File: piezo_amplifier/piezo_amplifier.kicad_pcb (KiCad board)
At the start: 2 copper layers, 40 x 23.5 mm, 22 parts, among them J1 Conn_01x02_Female, J2 Conn_01x02_Female, J3 Conn_01x02_Female, J4 Conn_01x02_Female, U1 LMV324, U2 TLV76033DBZT

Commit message: Add Logo on silkscreen
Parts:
- added G***: LOGO, Logos:asaurus_logo, B.Cu at (132.9, 77.2)
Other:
- board text added: "PiezoSaurus V1.0"
- board text removed: "Asaurus"
- board text removed: "Piezoelectric Probe Amplifier V1.0"

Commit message: PCB and schematics files finished, ready for release.
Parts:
- removed J2: Conn_01x02_Female, Connector_JST:JST_XH_S02B-XH-A_1x02_P2.50mm_Horizontal
- removed the REF** at (141.0, 91.0)
- removed the REF** at (109.0, 75.5)
- added C7: 22nF, Capacitor_SMD:C_0603_1608Metric, F.Cu at (113.8, 80.8)
- added C8: 22nF, Capacitor_SMD:C_0603_1608Metric, F.Cu at (116.2, 80.8)
- added C9: 1uF, Capacitor_SMD:C_0603_1608Metric, F.Cu at (122.0, 84.0)
- added D2: TVS_5V, Diode_SMD:D_SOD-123, F.Cu at (116.2, 76.0)
- added D3: LED, LED_SMD:LED_0603_1608Metric, F.Cu at (119.5, 63.2)
- added J5: Conn_01x02_Female, Connector_JST:JST_XH_S2B-XH-A_1x02_P2.50mm_Horizontal, F.Cu at (109.0, 66.7)
- added J6: Conn_01x02_Female, Connector_JST:JST_XH_S2B-XH-A_1x02_P2.50mm_Horizontal, F.Cu at (109.0, 84.4)
- added POT2: TC33X-2-103E, Potentiometer_SMD:Potentiometer_Bourns_TC33X_Vertical, F.Cu at (133.0, 69.0)
- added R10: 0R, Resistor_SMD:R_0603_1608Metric, F.Cu at (131.8, 90.5)
- added R7: 330, Resistor_SMD:R_0603_1608Metric, F.Cu at (121.5, 63.2)
- added R8: 330R, Resistor_SMD:R_0603_1608Metric, F.Cu at (126.0, 84.0)
- added R9: 0R, Resistor_SMD:R_0603_1608Metric, F.Cu at (131.8, 83.5)
- added REF**: MountingHole_2.5mm, MountingHole:MountingHole_2.5mm, F.Cu at (125.0, 64.0)
- added REF**: MountingHole_2.5mm, MountingHole:MountingHole_2.5mm, F.Cu at (125.0, 90.0)
- added TP1: TestPoint, TestPoint:TestPoint_Loop_D1.80mm_Drill1.0mm_Beaded, F.Cu at (118.0, 87.8)
- added TP2: TestPoint, TestPoint:TestPoint_Loop_D1.80mm_Drill1.0mm_Beaded, F.Cu at (115.5, 87.8)
- added TP3: TestPoint, TestPoint:TestPoint_Loop_D1.80mm_Drill1.0mm_Beaded, F.Cu at (122.5, 70.0)
- added TP4: TestPoint, TestPoint:TestPoint_Loop_D1.80mm_Drill1.0mm_Beaded, F.Cu at (114.2, 64.8)
- added TP5: TestPoint, TestPoint:TestPoint_Loop_D1.80mm_Drill1.0mm_Beaded, F.Cu at (125.0, 70.0)
- added TP6: TestPoint, TestPoint:TestPoint_Loop_D1.80mm_Drill1.0mm_Beaded, F.Cu at (127.5, 70.0)
- added U3: TLP185, Package_SO:SOIC-4_4.55x3.7mm_P2.54mm, F.Cu at (132.0, 87.0)
- J1, J3, J4: footprint Connector_JST:JST_XH_S02B-XH-A_1x02_P2.50mm_Horizontal -> Connector_JST:JST_XH_S2B-XH-A_1x02_P2.50mm_Horizontal
- POT1: value TC33X-2-103E -> 10K; footprint digikey-footprints:Trimpot_3.8mmx3.6mm_TC33X-2-103E -> Potentiometer_SMD:Potentiometer_Bourns_TC33X_Vertical
- R3: value 10K -> 330
- R4: value 10K -> 20K
- R6: value 100 -> 10K
- U2: footprint digikey-footprints:SOT-23-3 -> Package_TO_SOT_SMD:SOT-23
- moved POT1 27.2 mm to (117.0, 69.0), turned to 90 degrees
- moved J1 26.2 mm to (141.0, 69.0), turned to 90 degrees
- moved R6 25.3 mm to (113.8, 77.5), turned to 270 degrees
- moved C6 20.5 mm to (119.8, 74.2), turned to 270 degrees
- moved R5 20.4 mm to (136.0, 68.0)
- moved C1 20.3 mm to (136.9, 63.2), turned to 270 degrees
- moved C5 19.8 mm to (129.4, 63.2)
- moved C3 19.8 mm to (131.4, 63.2)
- moved C4 17.0 mm to (133.2, 74.2)
- moved R4 16.2 mm to (130.2, 74.2)
- moved R1 15.8 mm to (119.8, 77.5)
- moved U2 15.7 mm to (134.2, 63.2), turned to 90 degrees
- moved R3 15.2 mm to (130.2, 77.5)
- moved D1 14.1 mm to (130.2, 80.8), turned to 90 degrees
- moved J3 14.0 mm to (109.0, 75.6)
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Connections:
- J4 pad 1: GND -> Net-(J4-Pad1)
- POT1 pad 1: GND -> Net-(POT1-Pad1)
- POT1 pad 2: Net-(POT1-Pad2) -> Net-(C4-Pad2)
- POT1 pad 3: Net-(POT1-Pad2) -> Net-(C4-Pad2)
- R3 pad 1: Net-(C4-Pad2) -> Net-(D1-Pad2)
- R3 pad 2: Net-(J3-Pad2) -> Net-(R3-Pad2)
- R5 pad 2: Net-(POT1-Pad2) -> Net-(POT2-Pad2)
- R6 pad 1: Net-(R6-Pad1) -> Net-(C7-Pad2)
- R6 pad 2: Net-(D1-Pad2) -> Net-(J3-Pad2)
- U1 pad 1: Net-(C4-Pad1) -> Net-(POT1-Pad1)
- U1 pad 10: /Probe_Out -> Net-(POT2-Pad2)
- U1 pad 12: Net-(POT1-Pad2) -> /Vref
- U1 pad 13: Net-(C4-Pad1) -> Net-(C4-Pad2)
- U1 pad 14: /Probe_Out -> Net-(C4-Pad1)
- U1 pad 2: Net-(C4-Pad2) -> Net-(POT1-Pad1)
- U1 pad 3: /Vref -> Net-(C7-Pad2)
- U1 pad 8: Net-(R6-Pad1) -> Net-(R3-Pad2)
- U1 pad 9: Net-(R6-Pad1) -> Net-(C4-Pad1)
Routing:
- net /Vref: track 25.5 -> 53.6 mm, vias 0 -> 1
- net Net-(POT2-Pad2): track 0.00 -> 27.8 mm
- net Net-(C7-Pad2): track 0.00 -> 23.8 mm
- net Net-(J3-Pad2): track 6.68 -> 26.7 mm
- net /Probe_Out: track 28.4 -> 10.6 mm
- net /Vin: track 24.3 -> 7.57 mm
- net Net-(C4-Pad2): track 5.93 -> 20.7 mm, vias 0 -> 2
- net Net-(R3-Pad2): track 0.00 -> 14.3 mm
- net Net-(POT1-Pad1): track 0.00 -> 12.5 mm
- net Net-(C4-Pad1): track 10.2 -> 22.5 mm, vias 0 -> 1
- net Net-(J4-Pad1): track 0.00 -> 10.6 mm
- net Net-(POT1-Pad2): track 10.1 -> 0.00 mm
- net +3V3: track 39.7 -> 46.9 mm, vias 0 -> 2
- net GND: track 6.54 -> 0.00 mm, vias 2 -> 12
- net Net-(R6-Pad1): track 5.47 -> 0.00 mm
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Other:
- board size 40 x 23.5 mm -> 40 x 36 mm
- board text added: "Piezo Inputs"
- board text added: "PiezoSaurus V2.0"
- board text added: "Power On"
- board text added: "Sens Out"
- board text added: "Vin 5V-24V"
- board text removed: "PiezoSaurus V1.0"

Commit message: Version V2.0 released
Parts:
- removed G***: LOGO, Logos:asaurus_logo
- removed REF** (x2): MountingHole_2.5mm, MountingHole:MountingHole_2.5mm
- J1, J3, J4, J5, J6: value Conn_01x02_Female -> S2B-XH-A-1
- POT1: value 10K -> 10K_SMD; footprint Potentiometer_SMD:Potentiometer_Bourns_TC33X_Vertical -> digikey-footprints:Trimpot_3.8mmx3.6mm_TC33X-2-103E
- POT2: value TC33X-2-103E -> 10K_SMD; footprint Potentiometer_SMD:Potentiometer_Bourns_TC33X_Vertical -> digikey-footprints:Trimpot_3.8mmx3.6mm_TC33X-2-103E
- U2: value TLV76033DBZT -> TLV76033; footprint Package_TO_SOT_SMD:SOT-23 -> digikey-footprints:SOT-23-3
- moved J3 9.10 mm to (109.0, 66.5)
- moved J5 8.80 mm to (109.0, 75.5)
- moved J6 0.10 mm to (109.0, 84.5)
- turned POT1 to 0 degrees
- turned POT2 to 0 degrees

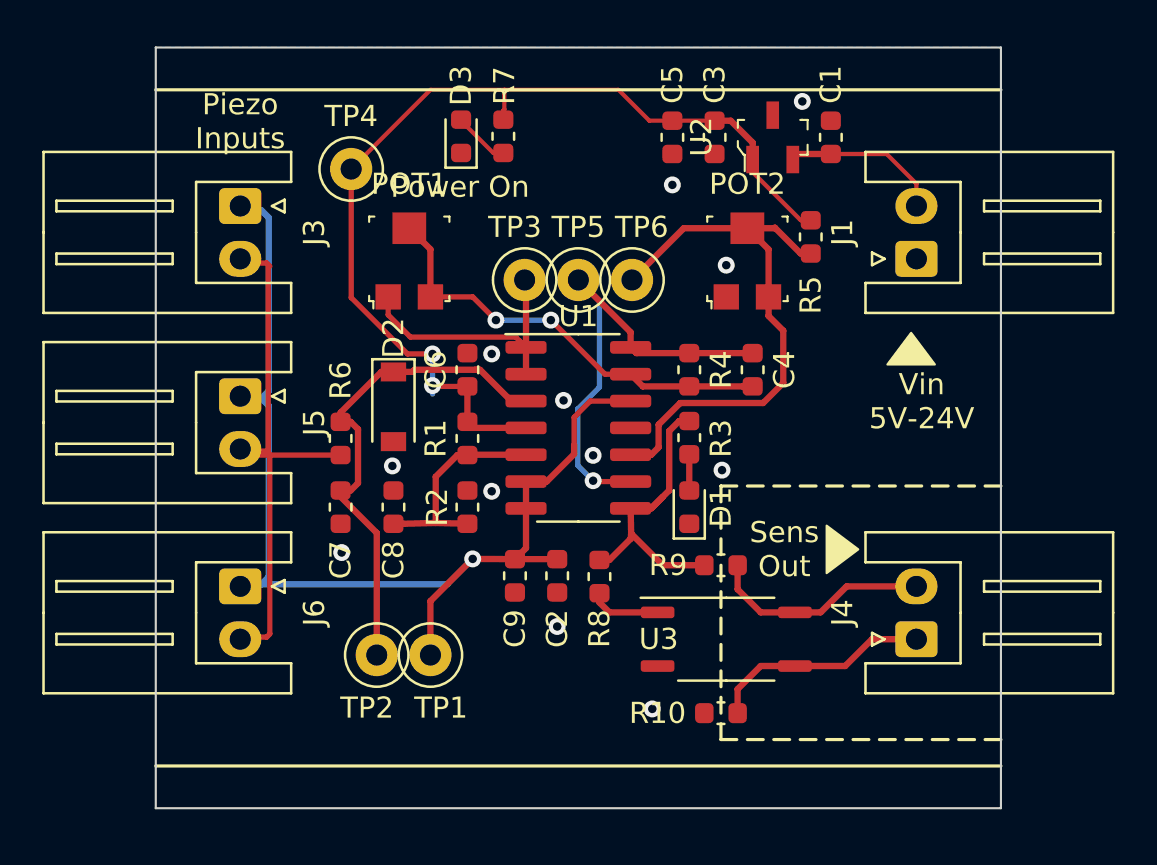
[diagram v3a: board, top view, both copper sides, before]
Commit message: Piezo amplifier V2.0 released. Updated with the new library convention to show not installed components and standardizing fields.
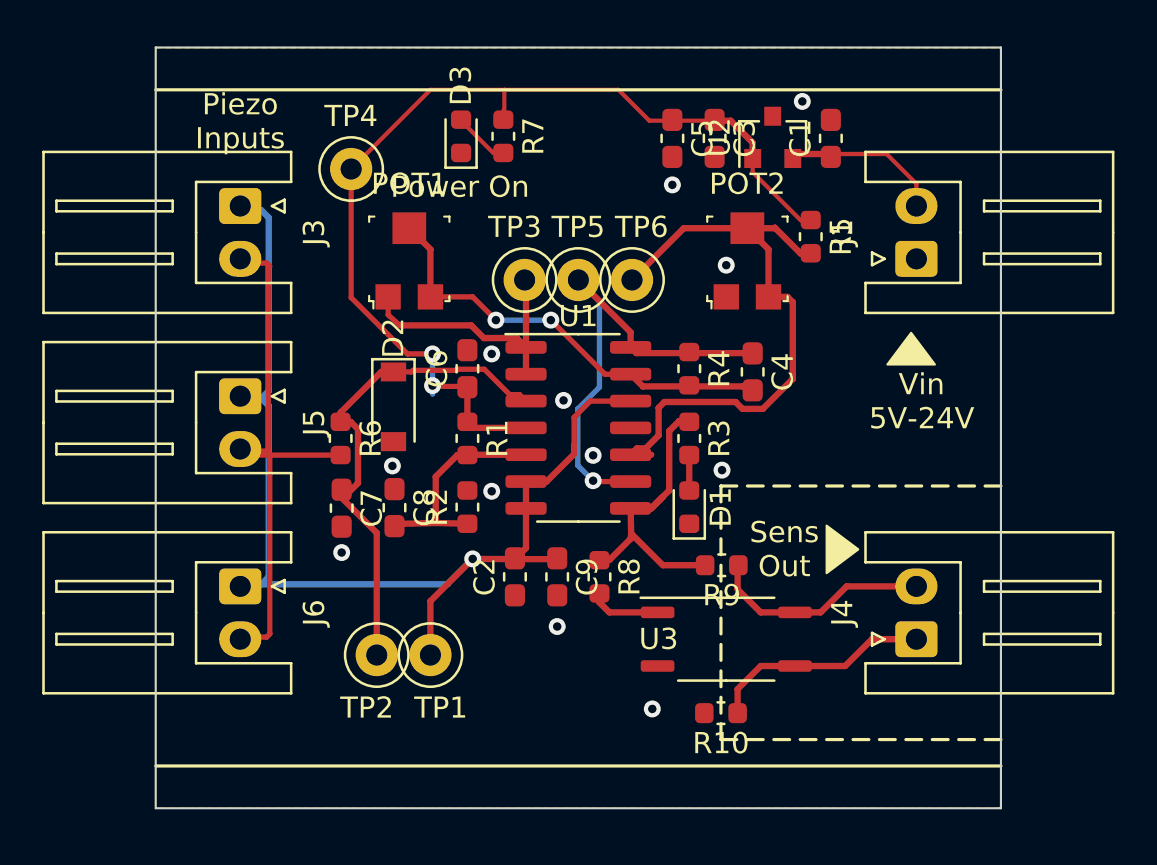
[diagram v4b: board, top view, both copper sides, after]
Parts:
- C1, C2, C3, C4, C5, C7, C8, C9: footprint Capacitor_SMD:C_0603_1608Metric -> Capacitor_SMD:C_0603_1608Metric_Pad1.05x0.95mm_HandSolder
- C6: value 2nF -> 22nF; footprint Capacitor_SMD:C_0603_1608Metric -> Capacitor_SMD:C_0603_1608Metric_Pad1.05x0.95mm_HandSolder
- POT1, POT2: value 10K_SMD -> 10K
- R3, R7: value 330 -> 330R
- U2: footprint digikey-footprints:SOT-23-3 -> Package_TO_SOT_SMD:SOT-23
- moved C2 2.00 mm to (122.0, 84.0)
- moved C9 2.00 mm to (124.0, 84.0), turned to 270 degrees
- moved C4 0.10 mm to (133.2, 74.3)
- moved C7 0.07 mm to (113.8, 80.8), turned to 270 degrees
- moved C8 0.06 mm to (116.3, 80.8)
- turned C1 to 90 degrees
- turned C5 to 270 degrees
- turned C6 to 90 degrees
- turned R3 to 270 degrees
- turned R9 to 180 degrees
- turned R8 to 270 degrees
- turned R10 to 180 degrees
- turned R7 to 270 degrees
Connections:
- C1 pad 1: GND -> /Vin
- C1 pad 2: /Vin -> GND
- C5 pad 1: GND -> +3V3
- C5 pad 2: +3V3 -> GND
- C6 pad 1: GND -> +3V3
- C6 pad 2: +3V3 -> GND
- C7 pad 1: GND -> Net-(C7-Pad1)
- C7 pad 2: Net-(C7-Pad2) -> GND
- C9 pad 1: GND -> /Vref
- C9 pad 2: /Vref -> GND
- D2 pad 1: Net-(C7-Pad2) -> Net-(C7-Pad1)
- R10 pad 1: GND -> Net-(J4-Pad1)
- R10 pad 2: Net-(J4-Pad1) -> GND
- R3 pad 1: Net-(D1-Pad2) -> Net-(R3-Pad1)
- R3 pad 2: Net-(R3-Pad2) -> Net-(D1-Pad2)
- R6 pad 1: Net-(C7-Pad2) -> Net-(C7-Pad1)
- R7 pad 1: Net-(D3-Pad2) -> +3V3
- R7 pad 2: +3V3 -> Net-(D3-Pad2)
- R8 pad 1: Net-(R8-Pad1) -> Net-(R3-Pad1)
- R8 pad 2: Net-(R3-Pad2) -> Net-(R8-Pad2)
- R9 pad 1: Net-(R3-Pad2) -> /Probe_Out
- R9 pad 2: /Probe_Out -> Net-(R3-Pad1)
- TP2 pad 1: Net-(C7-Pad2) -> Net-(C7-Pad1)
- U1 pad 3: Net-(C7-Pad2) -> Net-(C7-Pad1)
- U1 pad 8: Net-(R3-Pad2) -> Net-(R3-Pad1)
- U3 pad 1: Net-(R8-Pad1) -> Net-(R8-Pad2)
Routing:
- net Net-(C7-Pad2): track 23.8 -> 0.00 mm
- net Net-(C7-Pad1): track 0.00 -> 23.7 mm
- net Net-(R3-Pad2): track 14.3 -> 0.00 mm
- net Net-(R3-Pad1): track 0.00 -> 14.3 mm
- net Net-(R8-Pad2): track 0.00 -> 3.13 mm
- net Net-(R8-Pad1): track 3.13 -> 0.00 mm
- net Net-(POT2-Pad2): track 27.8 -> 30.2 mm

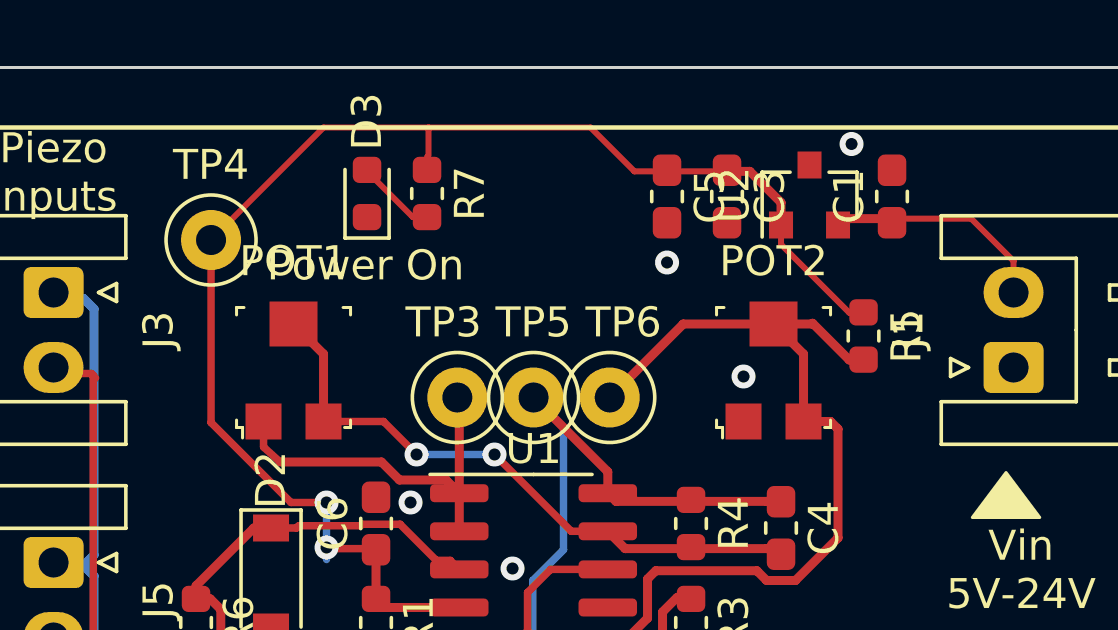
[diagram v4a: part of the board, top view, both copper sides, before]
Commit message: fixup! Piezo amplifier V2.0 released. Updated with the new library convention to show not installed components and standardizing fields.
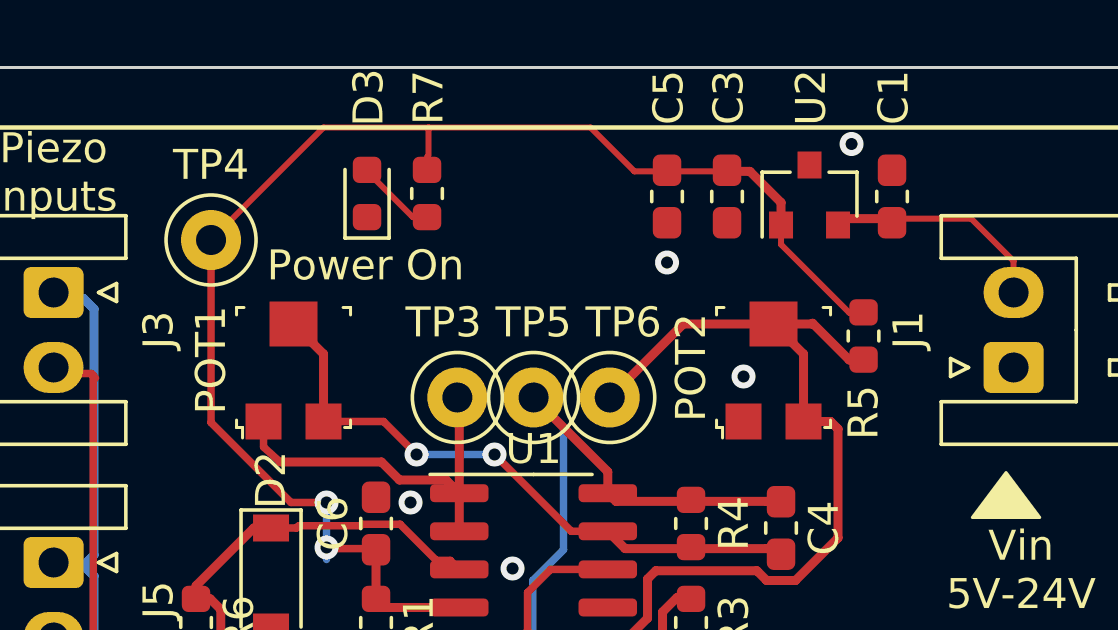
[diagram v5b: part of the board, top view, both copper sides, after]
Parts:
- added G***: LOGO, Logos:asaurus_logo, B.Cu at (125.0, 77.2)
